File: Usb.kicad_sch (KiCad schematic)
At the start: 0 parts

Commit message: Usb düzenlendi.
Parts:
- added C15, C29: 1uF, symbol Device:C
- added J3: USB_C_Receptacle_USB2.0_14P, symbol Connector:USB_C_Receptacle_USB2.0_14P
- added R13, R2: 5.1k, symbol Device:R
- added U4: USBLC6-2SC6, Package_TO_SOT_SMD:SOT-23-6, symbol Power_Protection:USBLC6-2SC6
- added U5: TLV75733PDRV, Package_SON:WSON-6-1EP_2x2mm_P0.65mm_EP1x1.6mm, symbol Regulator_Linear:TLV75733PDRV
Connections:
- new net: J3.A7 (D-), J3.B7 (D-), U4.4 (I/O2)
- new net: J3.A6 (D+), J3.B6 (D+), U4.6 (I/O1)
- new net: J3.B5 (CC2), R2.1
- new net: J3.A5 (CC1), R13.1
- new net GND: C15.2, C29.2, J3.A1 (GND), J3.A12 (GND), J3.B1 (GND), J3.B12 (GND), J3.SH (SHIELD), R13.2, R2.2, U4.2 (GND), U5.3 (GND), U5.7 (GND)
- new net USB_3V3: C29.1, U5.1 (OUT)
- new net USB_DM: U4.3 (I/O2)
- new net USB_DP: U4.1 (I/O1)
- new net USB_VBUS: C15.1, J3.A4 (VBUS), J3.A9 (VBUS), J3.B4 (VBUS), J3.B9 (VBUS), U5.4 (EN), U5.6 (IN)

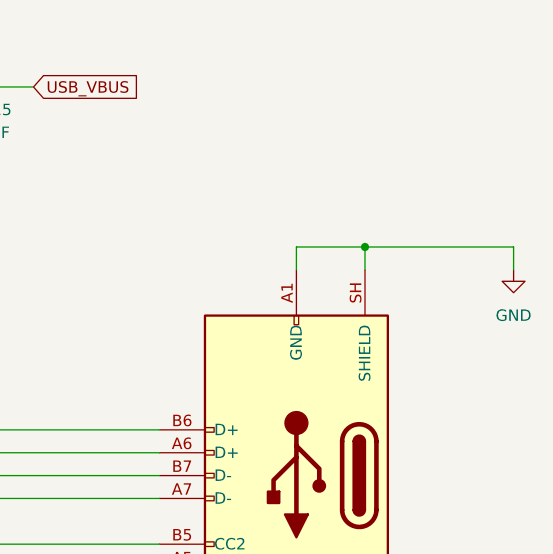
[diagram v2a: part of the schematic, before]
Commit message: Sdram ve power kaldırıldı.
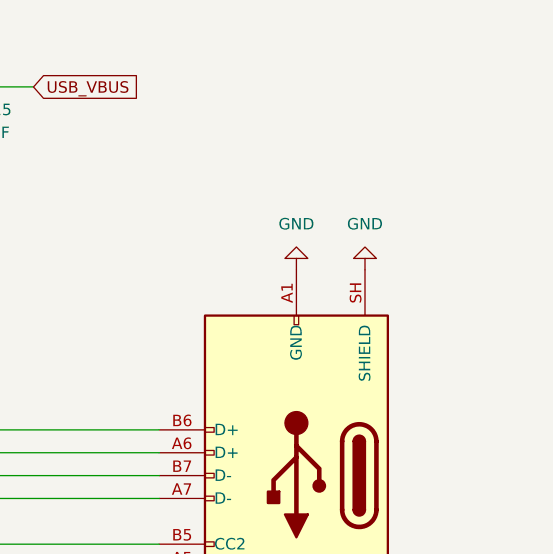
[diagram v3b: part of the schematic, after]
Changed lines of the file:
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@@
-	)
-	(junction
-		(at 170.18 73.66)
-		(diameter 0)
-		(color 0 0 0 0)
 	)
 	(junction
@@
 	(wire
 		(pts
-			(xy 162.56 76.2) (xy 162.56 73.66)
-		)
-		(stroke
-			(width 0)
-			(type default)
-		)
-	)
-	(wire
-		(pts
 			(xy 114.3 111.76) (xy 114.3 106.68)
 		)
@@
 	(wire
 		(pts
-			(xy 170.18 73.66) (xy 186.69 73.66)
-		)
-		(stroke
-			(width 0)
-			(type default)
-		)
-	)
-	(wire
-		(pts
-			(xy 162.56 73.66) (xy 170.18 73.66)
-		)
-		(stroke
-			(width 0)
-			(type default)
-		)
-	)
-	(wire
-		(pts
 			(xy 123.19 109.22) (xy 147.32 109.22)
 		)
@@
 	(wire
 		(pts
-			(xy 170.18 73.66) (xy 170.18 76.2)
-		)
-		(stroke
-			(width 0)
-			(type default)
-		)
-	)
-	(wire
-		(pts
 			(xy 147.32 93.98) (xy 114.3 93.98)
-		)
-		(stroke
-			(width 0)
-			(type default)
-		)
-	)
-	(wire
-		(pts
-			(xy 186.69 73.66) (xy 186.69 76.2)
 		)
 		(stroke
@@
 	(symbol
 		(lib_id "power:GND")
-		(at 186.69 76.2 0)
-		(unit 1)
-		(body_style 1)
-		(exclude_from_sim no)
-		(in_bom yes)
-		(on_board yes)
-		(in_pos_files yes)
-		(dnp no)
-		(fields_autoplaced yes)
-		(property "Reference" "#PWR010"
-			(at 186.69 82.55 0)
-			(hide yes)
-			(show_name no)
-			(do_not_autoplace no)
-			(effects
-				(font
-					(size 1.27 1.27)
-				)
-			)
-		)
-		(property "Value" "GND"
-			(at 186.69 81.28 0)
-			(show_name no)
-			(do_not_autoplace no)
-			(effects
-				(font
-					(size 1.27 1.27)
-				)
-			)
-		)
-		(property "Footprint" ""
-			(at 186.69 76.2 0)
-			(hide yes)
-			(show_name no)
-			(do_not_autoplace no)
-			(effects
-				(font
-					(size 1.27 1.27)
-				)
-			)
-		)
-		(property "Datasheet" ""
-			(at 186.69 76.2 0)
-			(hide yes)
-			(show_name no)
-			(do_not_autoplace no)
-			(effects
-				(font
-					(size 1.27 1.27)
-				)
-			)
-		)
-		(property "Description" "Power symbol creates a global label with name \"GND\" , ground"
-			(at 186.69 76.2 0)
-			(hide yes)
-			(show_name no)
-			(do_not_autoplace no)
-			(effects
-				(font
-					(size 1.27 1.27)
-				)
-			)
-		)
-		(pin "1"
-		)
-		(instances
-			(project "Ukk"
-				(path "/2375ab6f-0d27-47c2-8e53-820af89ba359/5ed8c3c0-d4b3-4080-858e-bb8389e2c082"
-					(reference "#PWR010")
-					(unit 1)
-				)
-			)
-		)
-	)
-	(symbol
-		(lib_id "power:GND")
 		(at 97.79 66.04 0)
 		(unit 1)
@@
 	)
 	(symbol
+		(lib_id "power:GND")
+		(at 170.18 76.2 180)
+		(unit 1)
+		(body_style 1)
+		(exclude_from_sim no)
+		(in_bom yes)
+		(on_board yes)
+		(in_pos_files yes)
+		(dnp no)
+		(fields_autoplaced yes)
+		(property "Reference" "#PWR031"
+			(at 170.18 69.85 0)
+			(hide yes)
+			(show_name no)
+			(do_not_autoplace no)
+			(effects
+				(font
+					(size 1.27 1.27)
+				)
+			)
+		)
+		(property "Value" "GND"
+			(at 170.18 71.12 0)
+			(show_name no)
+			(do_not_autoplace no)
+			(effects
+				(font
+					(size 1.27 1.27)
+				)
+			)
+		)
+		(property "Footprint" ""
+			(at 170.18 76.2 0)
+			(hide yes)
+			(show_name no)
+			(do_not_autoplace no)
+			(effects
+				(font
+					(size 1.27 1.27)
+				)
+			)
+		)
+		(property "Datasheet" ""
+			(at 170.18 76.2 0)
+			(hide yes)
+			(show_name no)
+			(do_not_autoplace no)
+			(effects
+				(font
+					(size 1.27 1.27)
+				)
+			)
+		)
+		(property "Description" "Power symbol creates a global label with name \"GND\" , ground"
+			(at 170.18 76.2 0)
+			(hide yes)
+			(show_name no)
+			(do_not_autoplace no)
+			(effects
+				(font
+					(size 1.27 1.27)
+				)
+			)
+		)
+		(pin "1"
+		)
+		(instances
+			(project "Ukk"
+				(path "/2375ab6f-0d27-47c2-8e53-820af89ba359/5ed8c3c0-d4b3-4080-858e-bb8389e2c082"
+					(reference "#PWR031")
+					(unit 1)
+				)
+			)
+		)
+	)
+	(symbol
 		(lib_id "Device:R")
 		(at 123.19 115.57 0)
@@
 					(unit 1)
 				)
+			)
+		)
+	)
+	(symbol
+		(lib_id "power:GND")
+		(at 162.56 76.2 180)
+		(unit 1)
+		(body_style 1)
+		(exclude_from_sim no)
+		(in_bom yes)
+		(on_board yes)
+		(in_pos_files yes)
+		(dnp no)
+		(fields_autoplaced yes)
+		(property "Reference" "#PWR030"
+			(at 162.56 69.85 0)
+			(hide yes)
+			(show_name no)
+			(do_not_autoplace no)
+			(effects
+				(font
+					(size 1.27 1.27)
+				)
+			)
+		)
+		(property "Value" "GND"
+			(at 162.56 71.12 0)
+			(show_name no)
+			(do_not_autoplace no)
+			(effects
+				(font
+					(size 1.27 1.27)
+				)
+			)
+		)
+		(property "Footprint" ""
+			(at 162.56 76.2 0)
+			(hide yes)
+			(show_name no)
+			(do_not_autoplace no)
+			(effects
+				(font
+					(size 1.27 1.27)
+				)
+			)
+		)
+		(property "Datasheet" ""
+			(at 162.56 76.2 0)
+			(hide yes)
+			(show_name no)
+			(do_not_autoplace no)
+			(effects
+				(font
+					(size 1.27 1.27)
+				)
+			)
+		)
+		(property "Description" "Power symbol creates a global label with name \"GND\" , ground"
+			(at 162.56 76.2 0)
+			(hide yes)
+			(show_name no)
+			(do_not_autoplace no)
+			(effects
+				(font
+					(size 1.27 1.27)
+				)
+			)
+		)
+		(pin "1"
+		)
+		(instances
+			(project "Ukk"
+				(path "/2375ab6f-0d27-47c2-8e53-820af89ba359/5ed8c3c0-d4b3-4080-858e-bb8389e2c082"
+					(reference "#PWR030")
+					(unit 1)
+				)
